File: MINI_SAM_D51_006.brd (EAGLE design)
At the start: 24.1 x 39.2 mm, 32 parts, among them IC1 AP2112K-3.3V, IC2 PRTR5V0U2X, IC4 ATSAMD51G_TQFN48, J1 MOLEX_47346-100147346, J2 CORTEX_DEBUG_PTH, SW1 KMS233GLFG, SW2 KMS233GLFG, U1 GD25x16

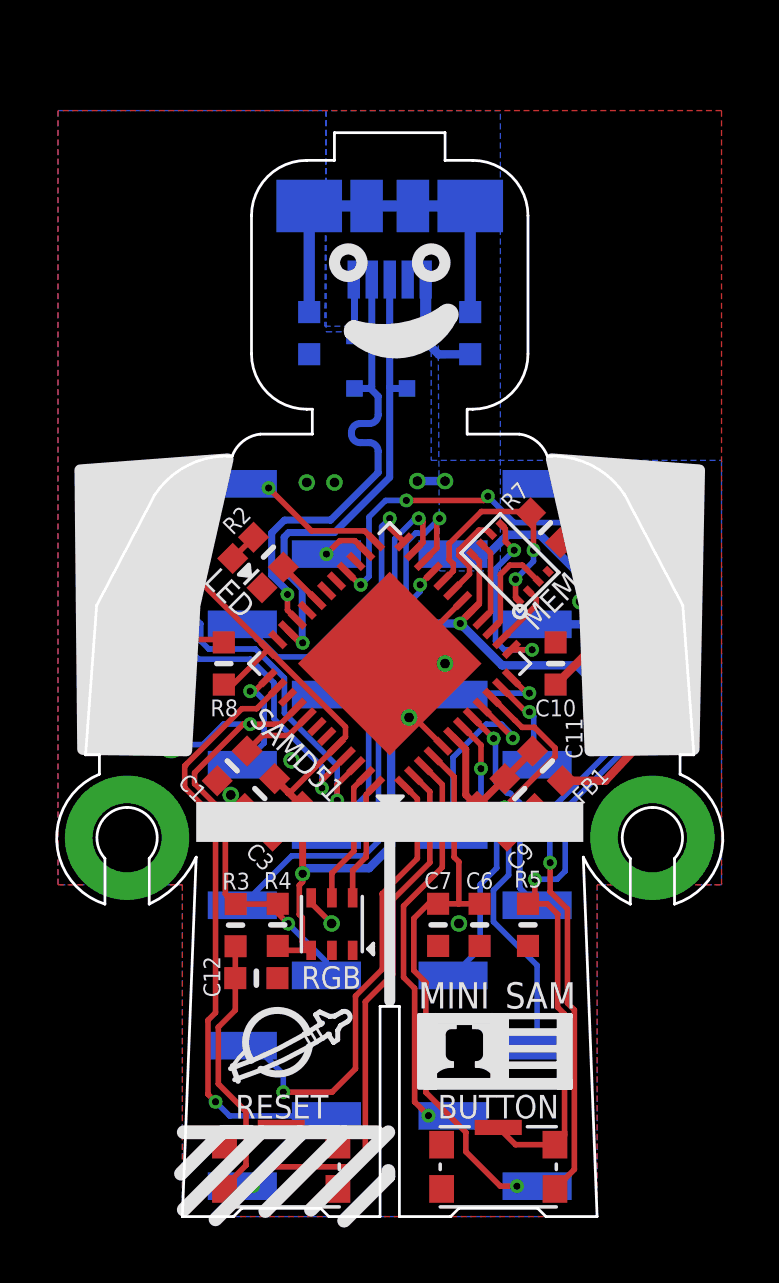
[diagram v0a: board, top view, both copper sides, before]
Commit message: Updated to 006
Mostly cosmetic updates, some associated component re-arranging.
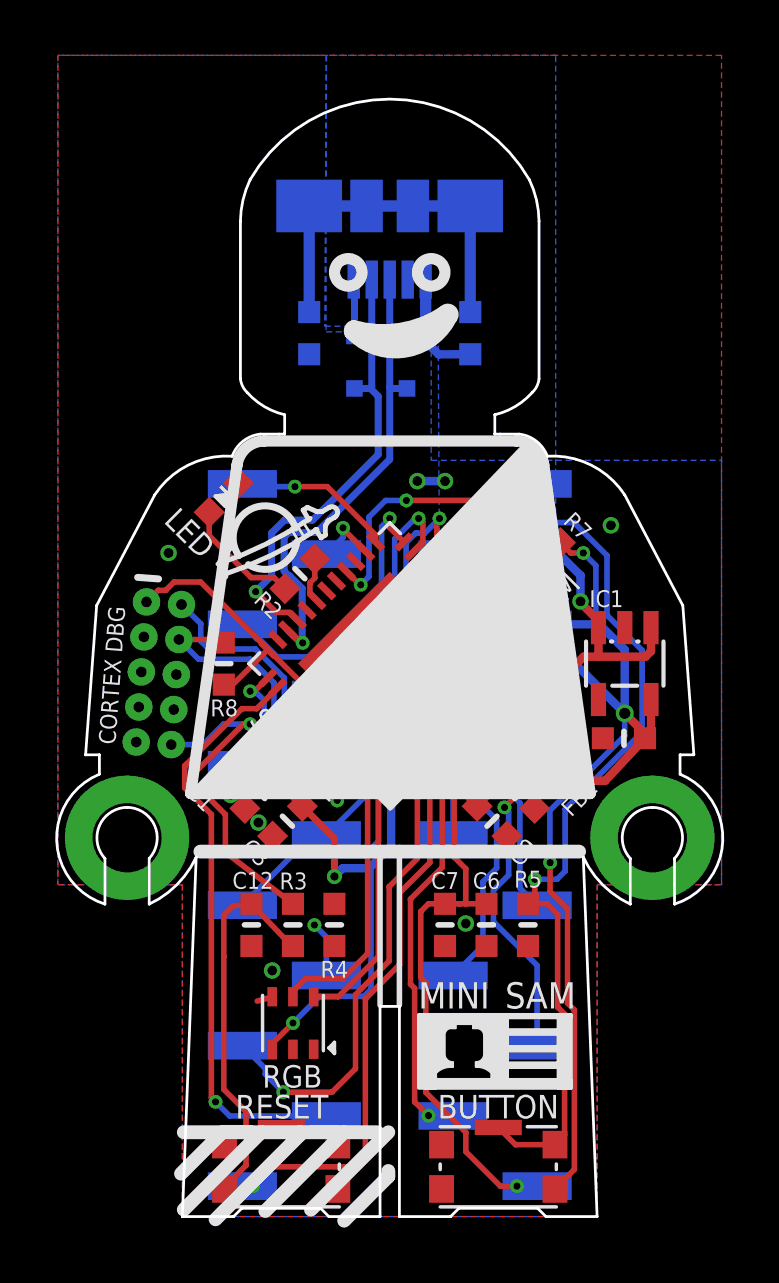
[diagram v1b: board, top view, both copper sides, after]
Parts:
- moved RGB 3.85 mm to (8.50, 7.00)
- moved LED 2.86 mm to (6.00, 26.0), turned to 315 degrees
- moved R3 2.08 mm to (8.50, 10.6)
- moved R4 2.05 mm to (10.0, 10.6), turned to 90 degrees
- moved C12 1.93 mm to (7.00, 10.6), turned to 90 degrees
- moved R2 1.38 mm to (8.75, 23.2), turned to 45 degrees
- moved C6 0.25 mm to (15.5, 10.6)
- moved C7 0.25 mm to (14.0, 10.6)
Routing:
- net DOTSTAR_CLK: track 4.93 -> 9.93 mm
- net DOTSTAR_DATA: track 4.41 -> 9.18 mm
- net VDD: track 82.3 -> 86.6 mm, vias 5 -> 6
- net N$4: track 9.78 -> 13.9 mm
- net N$3: track 1.08 -> 4.38 mm
- net !RESET: track 18.1 -> 16.3 mm
- net USBD-: track 17.2 -> 16.4 mm
- net GND: track 16.2 -> 15.5 mm, vias 15 -> 13
- net TX_D1: track 1.79 -> 2.40 mm
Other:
- board size 24.1 x 39.2 mm -> 24.1 x 40.4 mm

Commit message: More minor cosmetic changes
Minor updates to board design and cosmetic changes.
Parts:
- removed LED: (no value), microbuilder:CHIPLED_0603_NOOUTLINE
- added L: (no value), microbuilder:CHIPLED_0603_NOOUTLINE
- moved R2 3.64 mm to (5.35, 24.6), turned to 262 degrees
- moved R7 0.37 mm to (18.0, 25.0)
- moved U1 0.30 mm to (16.6, 23.6)
- renumbered FB1 to FB, IC1 to VREG
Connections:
- net GND: now also L.C; no longer LED.C
- net N$3: now also L.A; no longer LED.A
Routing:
- net N$3: track 4.38 -> 1.20 mm
- net D13: track 1.69 -> 4.75 mm
- net !RESET: track 16.3 -> 17.9 mm, vias 2 -> 3
- net GND: track 15.5 -> 14.3 mm
- net TX_D1: track 2.40 -> 1.68 mm
- net VDD: track 86.6 -> 87.1 mm, vias 6 -> 7
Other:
- board text added: "D51 build 006 2018"
- board text added: "STATUS"
- board text added: "build D51 006"
- board text removed: "build D51 005"
